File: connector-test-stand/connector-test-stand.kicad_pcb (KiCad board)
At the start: 2 copper layers, 99.1 x 99.1 mm, 81 parts, among them J1 Conn_01x02, J10 Conn_01x04_MountingPin, J11 Conn_01x03_MountingPin, J12 DVI-I_Dual_Link, J2 Conn_01x02, J3 Conn_01x02, J4 Conn_01x05, J5 Conn_01x04_MountingPin, J6 Conn_01x02, J7 Conn_01x03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

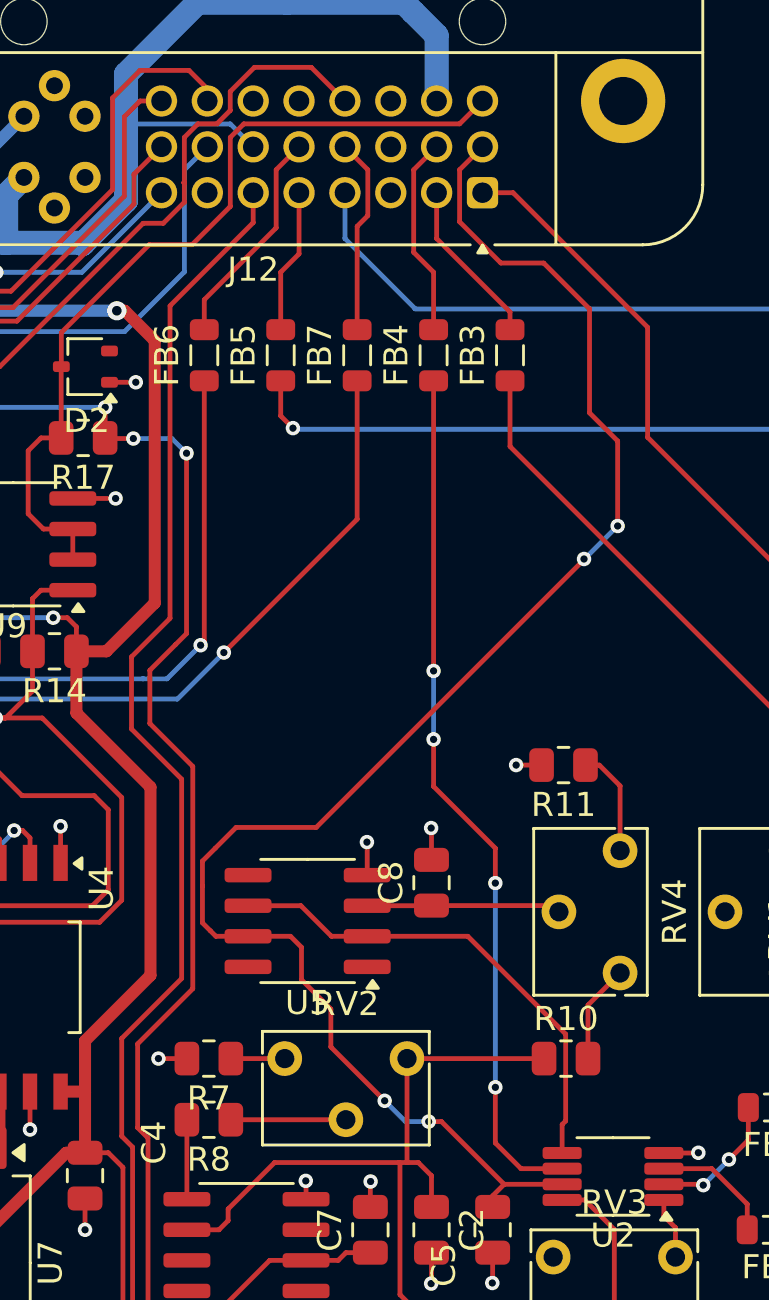
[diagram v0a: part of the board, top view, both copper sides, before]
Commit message: change strain power supply
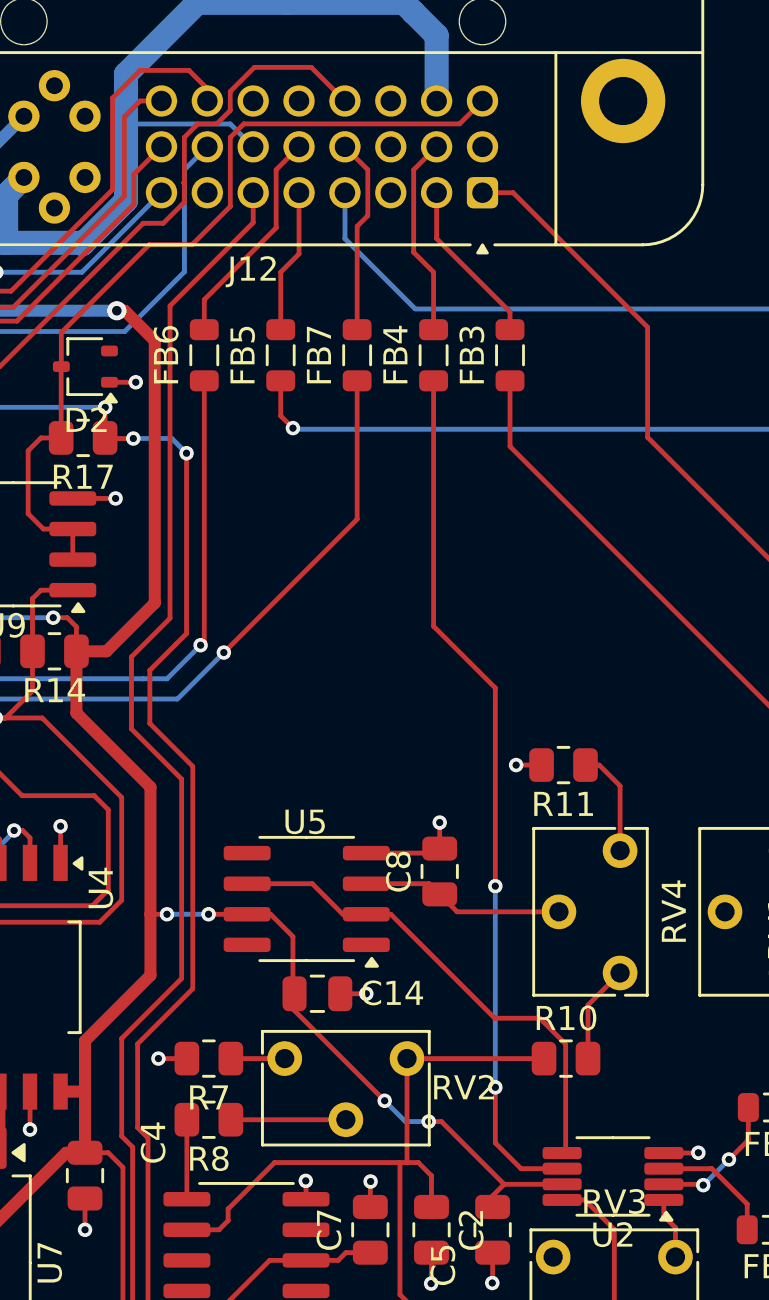
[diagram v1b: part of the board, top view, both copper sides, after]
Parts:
- added C14: C, Capacitor_SMD:C_0805_2012Metric, F.Cu at (348.0, 147.3)
- moved U5 0.92 mm to (347.5, 143.4)
- moved C8 0.58 mm to (353.1, 142.2)
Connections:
- C5 pad 1: STRAIN_GAUGE_POWER_SUPPLY -> +3.3V
- J12 pad 9: STRAIN_GAUGE_POWER_SUPPLY -> GND
- U2 pad 7: STRAIN_GAUGE_POWER_SUPPLY -> +3.3V
- U5 pad 7: STRAIN_GAUGE_POWER_SUPPLY -> +3.3V
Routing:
- net STRAIN_GAUGE_POWER_SUPPLY: track 67.8 -> 0.00 mm, vias 4 -> 0
- net +3.3V: track 305.1 -> 329.8 mm, vias 6 -> 10
- net GND: track 109.4 -> 111.8 mm
- net Net-(U5-+): track 8.07 -> 8.85 mm
- net STRAIN_GAUGE_RETURN: vias 4 -> 2

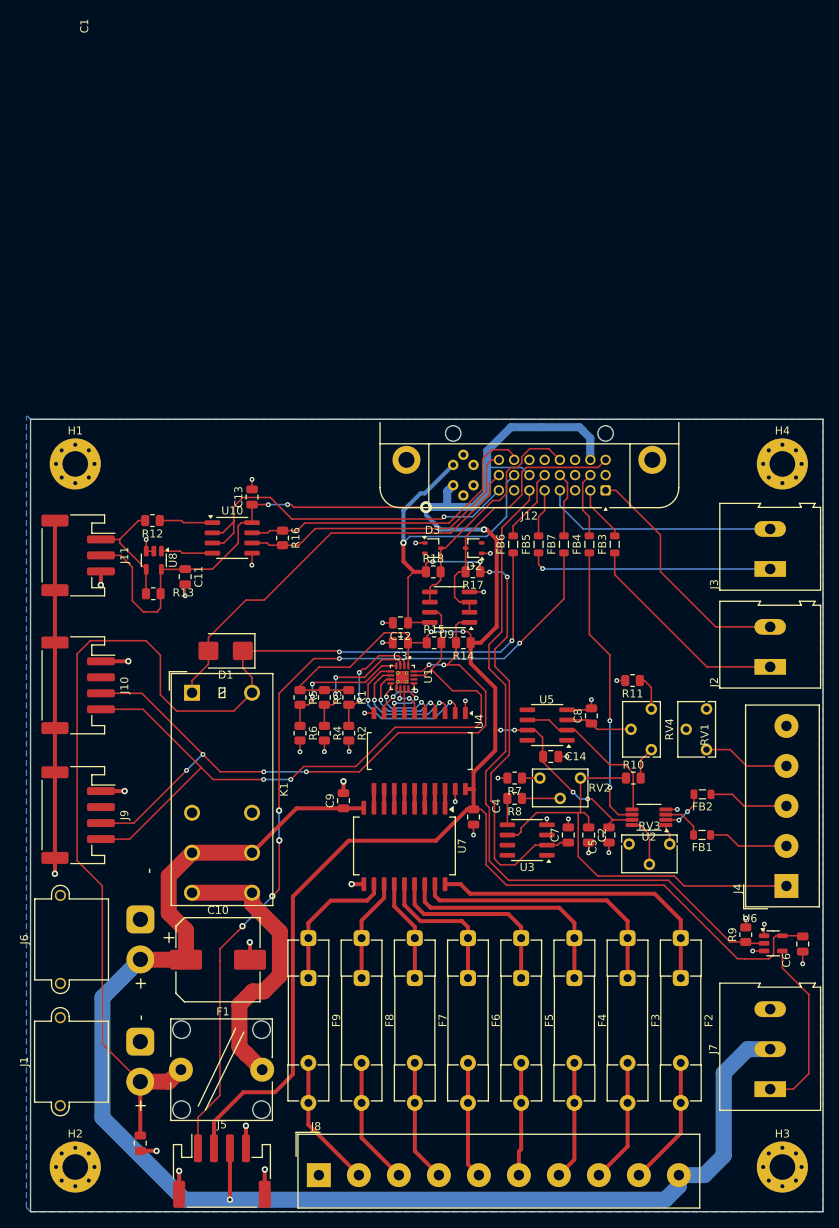
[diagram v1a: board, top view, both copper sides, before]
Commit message: Test stand board improve text, move conector too near border
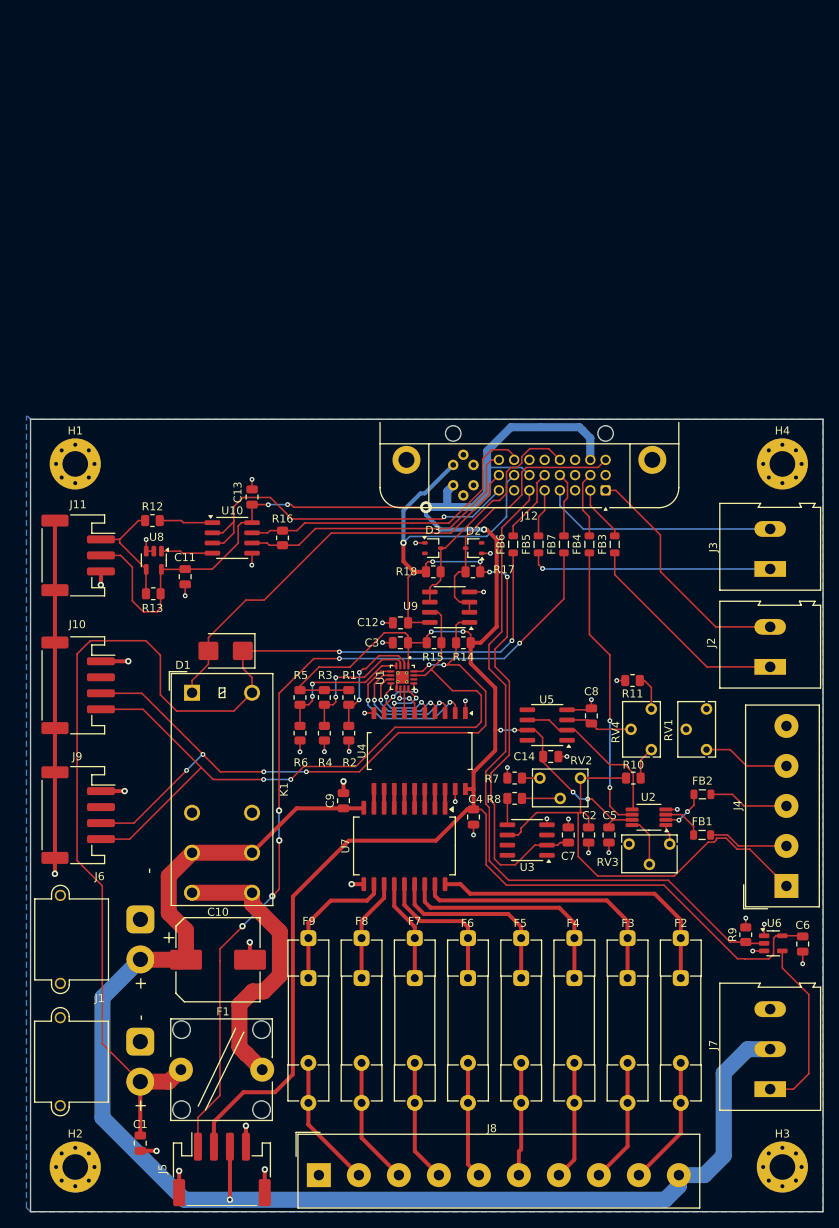
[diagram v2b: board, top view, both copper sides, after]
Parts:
- added G***: LOGO, shared:logo20x20, F.Cu at (361.9, 128.0)
- moved J5 0.20 mm to (306.9, 198.9)
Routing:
- net Net-(J4-Pin_1): track 56.2 -> 60.2 mm

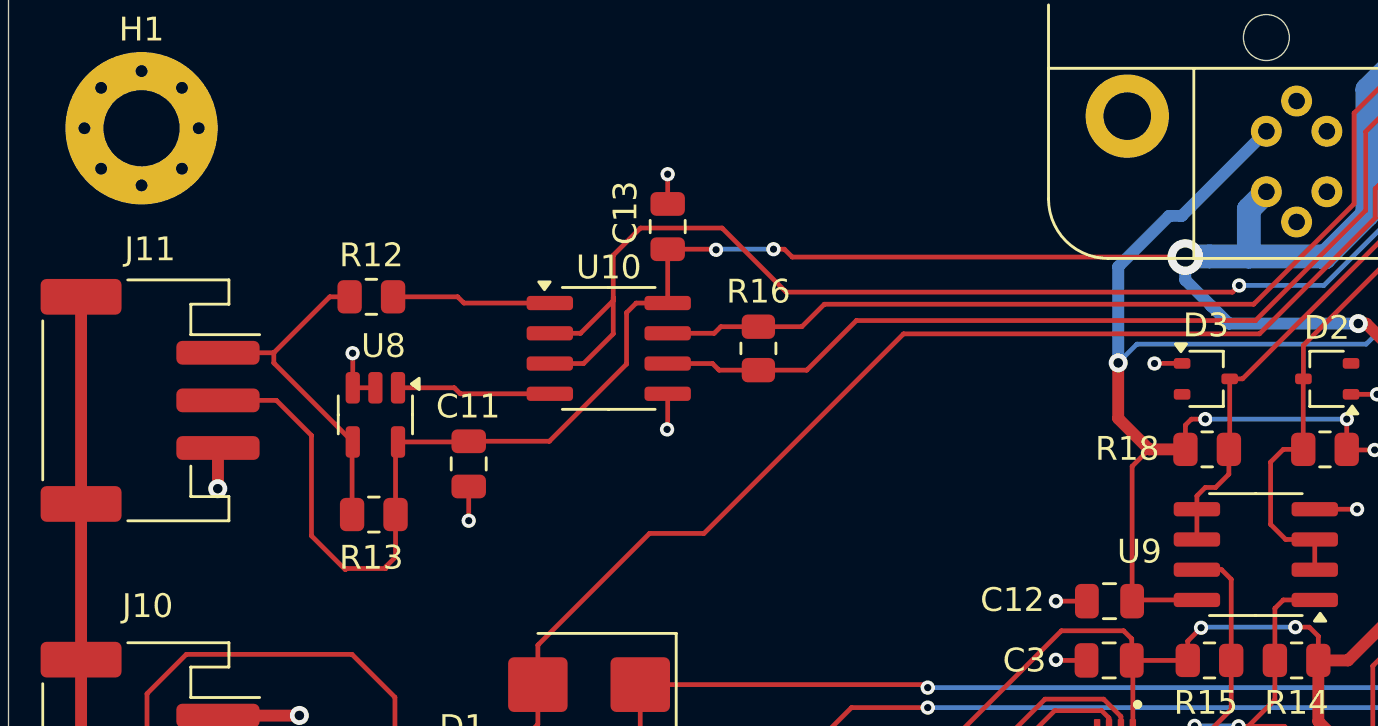
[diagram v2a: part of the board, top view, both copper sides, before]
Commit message: Fix uart connection, add crossing and enable negation
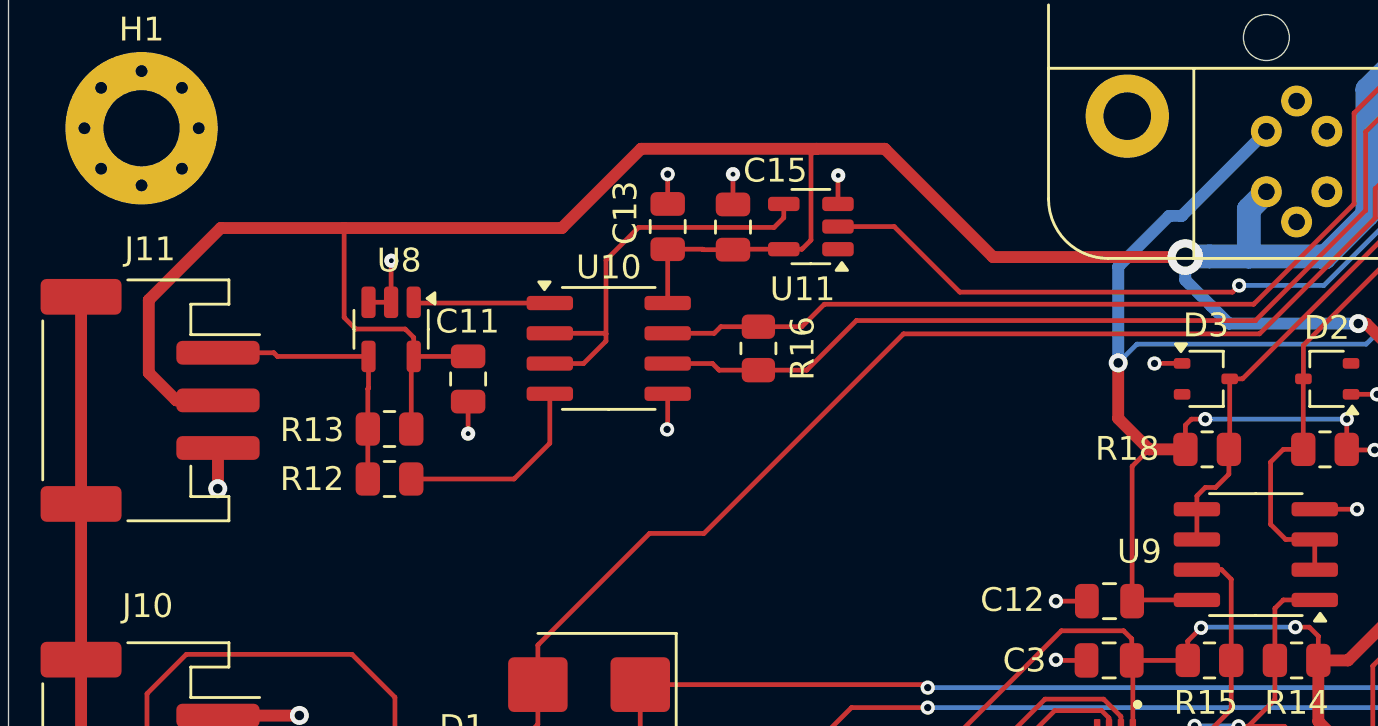
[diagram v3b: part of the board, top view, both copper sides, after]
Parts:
- added C15: C, Capacitor_SMD:C_0805_2012Metric, F.Cu at (313.4, 114.9)
- added U11: 74AHCT1G04, Package_TO_SOT_SMD:SOT-23-5, F.Cu at (316.7, 114.9)
- moved R12 7.69 mm to (299.0, 125.5)
- moved R13 3.65 mm to (299.0, 123.4)
- moved U8 3.65 mm to (299.0, 119.2)
- moved C11 3.57 mm to (302.3, 121.3)
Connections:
- U10 pad 1: RX -> TX
- U10 pad 2: RS485 transmit enable -> Net-(U10-DE)
- U10 pad 3: RS485 transmit enable -> Net-(U10-DE)
- U10 pad 4: TX -> RX
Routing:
- net +3.3V: track 329.8 -> 352.1 mm, vias 10 -> 8
- net RS485 transmit enable: track 46.1 -> 26.3 mm
- net Net-(U10-DE): track 0.00 -> 17.3 mm
- net Net-(J11-Pin_1): track 14.7 -> 11.5 mm
- net GND: track 111.9 -> 114.6 mm, vias 40 -> 42
- net RX: track 6.69 -> 8.52 mm
- net TX: track 6.48 -> 5.73 mm
